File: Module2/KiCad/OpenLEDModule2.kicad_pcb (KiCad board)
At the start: 2 copper layers, 29.2 x 53.1 mm, 11 parts, among them P1 CONN_01X02, P2 CONN_01X02

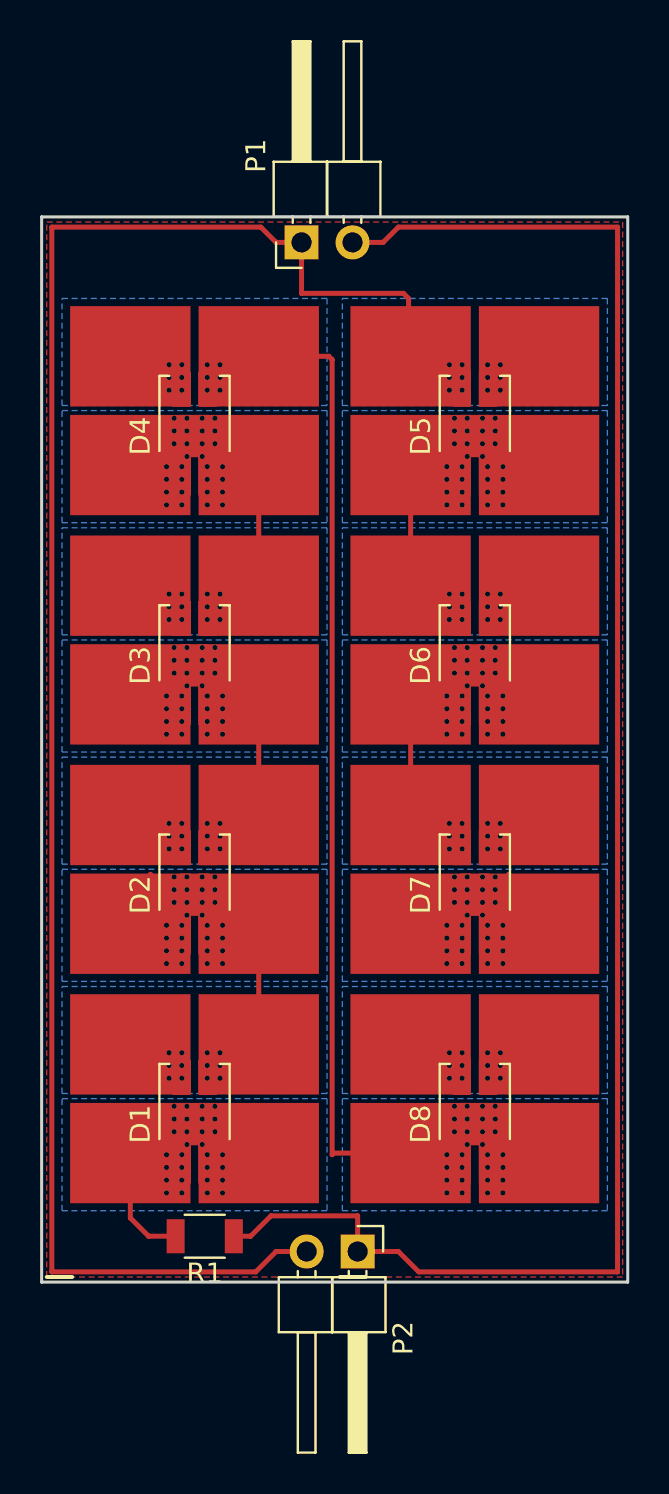
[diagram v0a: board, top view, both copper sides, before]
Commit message: Several fixes to resolve review comments (thermal via connections, cooling pads, footprint, past and mask layers, resistors, holes, tracks)
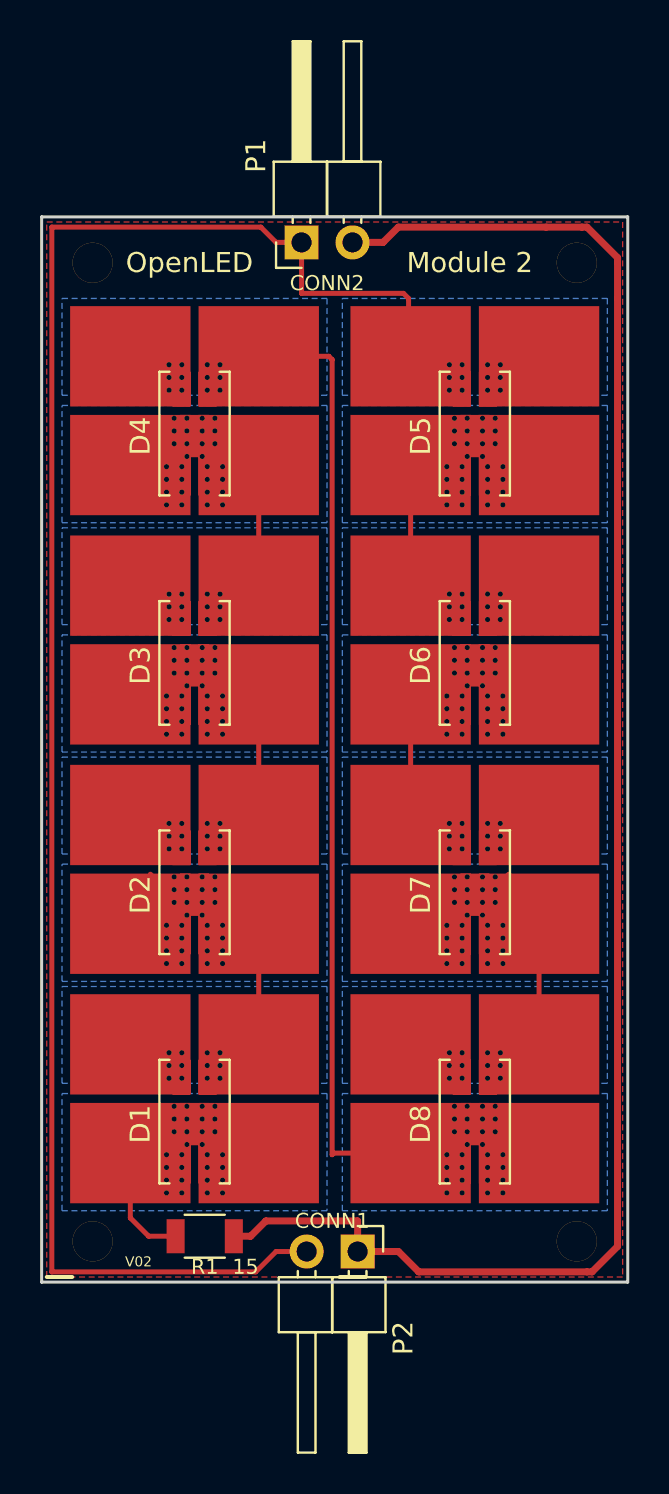
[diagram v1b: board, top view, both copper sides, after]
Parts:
- added ?: , OpenLed:DRILLHOLE, F.Cu at (156.5, 93.7)
- added ?: , OpenLed:DRILLHOLE, F.Cu at (156.5, 142.5)
- added ?: , OpenLed:DRILLHOLE, F.Cu at (132.3, 142.5)
- added ?: , OpenLed:DRILLHOLE, F.Cu at (132.3, 93.7)
- P1: value CONN_01X02 -> CONN2
- P2: value CONN_01X02 -> CONN1
- R1: value 14 -> 15
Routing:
- net Net-(D7-Pad2): track 1.47 -> 7.48 mm
- net +24V: track 87.3 -> 85.3 mm
- added copper zone on B.Cu, net GND
- added copper zone on B.Cu, net Net-(D1-Pad1)
- added copper zone on B.Cu, net Net-(D1-Pad2)
- added copper zone on B.Cu, net Net-(D2-Pad1)
- added copper zone on B.Cu, net Net-(D3-Pad1)
- added copper zone on B.Cu, net Net-(D4-Pad1)
- added copper zone on B.Cu, net Net-(D5-Pad2)
- added copper zone on B.Cu, net Net-(D6-Pad2)
- added copper zone on B.Cu, net Net-(D7-Pad2)
- removed copper zone on B.Cu, net (none)
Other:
- board text added: "V02"
- board text removed: "V001"
